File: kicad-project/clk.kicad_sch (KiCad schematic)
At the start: 7 parts, among them Q1 Q_NPN_BCE, U5 LM555xN

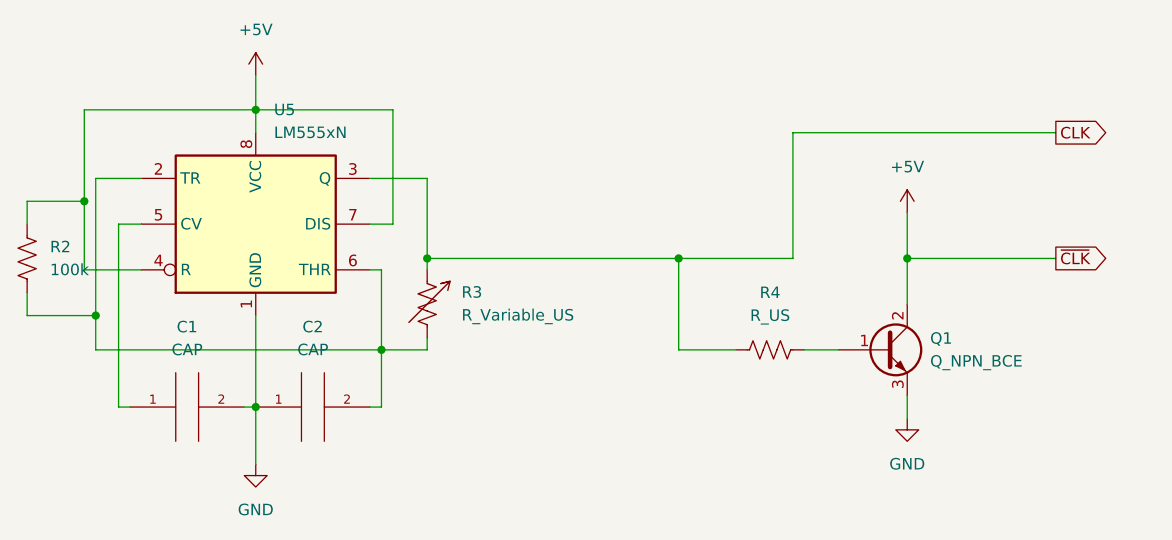
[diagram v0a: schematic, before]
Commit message: update schematic
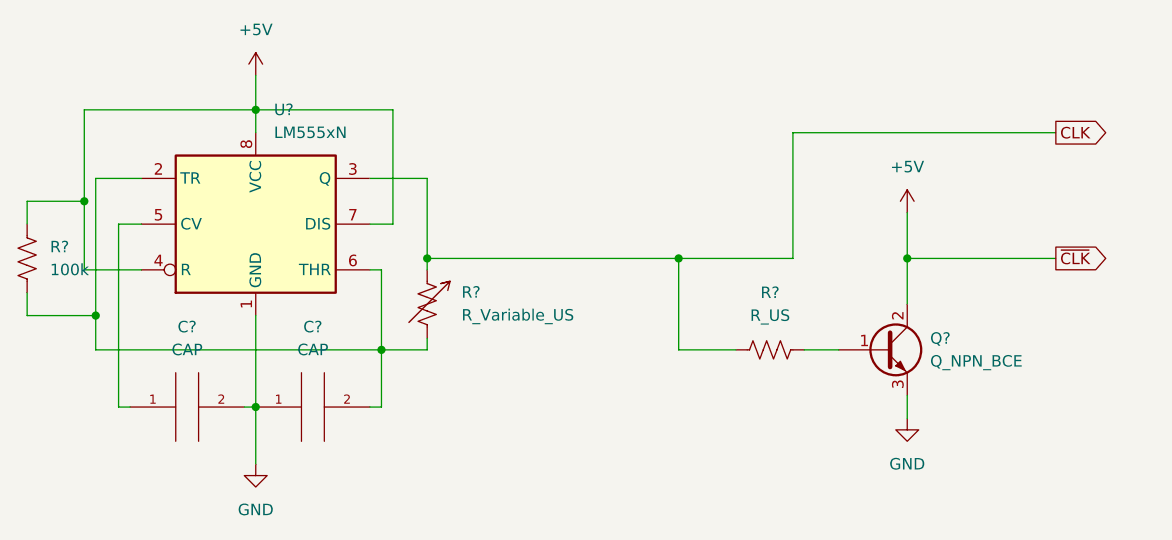
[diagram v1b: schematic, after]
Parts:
- renumbered C1 to C?, C2 to C?, Q1 to Q?, R3 to R?, R4 to R?, R2 to R?, U5 to U?
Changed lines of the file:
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@@
   (symbol (lib_id "power:GND") (at 152.4 128.27 0) (unit 1)
     (in_bom yes) (on_board yes) (fields_autoplaced)
-    (property "Reference" "#PWR0114" (id 0) (at 152.4 134.62 0)
+    (property "Reference" "#PWR0128" (id 0) (at 152.4 134.62 0)
       (effects (font (size 1.27 1.27)) hide)
     )
@@
   (symbol (lib_id "Timer:LM555xN") (at 152.4 101.6 0) (unit 1)
     (in_bom yes) (on_board yes) (fields_autoplaced)
-    (property "Reference" "U5" (id 0) (at 154.4194 88.9 0)
+    (property "Reference" "U?" (id 0) (at 154.4194 88.9 0)
       (effects (font (size 1.27 1.27)) (justify left))
     )
@@
   (symbol (lib_id "Device:R_Variable_US") (at 171.45 110.49 0) (unit 1)
     (in_bom yes) (on_board yes) (fields_autoplaced)
-    (property "Reference" "R3" (id 0) (at 175.26 109.1818 0)
+    (property "Reference" "R?" (id 0) (at 175.26 109.1818 0)
       (effects (font (size 1.27 1.27)) (justify left))
     )
@@
   (symbol (lib_id "Device:R_US") (at 209.55 115.57 90) (unit 1)
     (in_bom yes) (on_board yes) (fields_autoplaced)
-    (property "Reference" "R4" (id 0) (at 209.55 109.22 90))
+    (property "Reference" "R?" (id 0) (at 209.55 109.22 90))
     (property "Value" "R_US" (id 1) (at 209.55 111.76 90))
     (property "Footprint" "" (id 2) (at 209.804 114.554 90)
@@
   (symbol (lib_id "pspice:CAP") (at 144.78 121.92 90) (unit 1)
     (in_bom yes) (on_board yes) (fields_autoplaced)
-    (property "Reference" "C1" (id 0) (at 144.78 113.03 90))
+    (property "Reference" "C?" (id 0) (at 144.78 113.03 90))
     (property "Value" "CAP" (id 1) (at 144.78 115.57 90))
     (property "Footprint" "" (id 2) (at 144.78 121.92 0)
@@
   (symbol (lib_id "Device:Q_NPN_BCE") (at 222.25 115.57 0) (unit 1)
     (in_bom yes) (on_board yes) (fields_autoplaced)
-    (property "Reference" "Q1" (id 0) (at 227.33 114.2999 0)
+    (property "Reference" "Q?" (id 0) (at 227.33 114.2999 0)
       (effects (font (size 1.27 1.27)) (justify left))
     )
@@
   (symbol (lib_id "power:+5V") (at 224.79 100.33 0) (unit 1)
     (in_bom yes) (on_board yes) (fields_autoplaced)
-    (property "Reference" "#PWR0111" (id 0) (at 224.79 104.14 0)
+    (property "Reference" "#PWR0126" (id 0) (at 224.79 104.14 0)
       (effects (font (size 1.27 1.27)) hide)
     )
@@
   (symbol (lib_id "power:GND") (at 224.79 123.19 0) (unit 1)
     (in_bom yes) (on_board yes) (fields_autoplaced)
-    (property "Reference" "#PWR0112" (id 0) (at 224.79 129.54 0)
+    (property "Reference" "#PWR0125" (id 0) (at 224.79 129.54 0)
       (effects (font (size 1.27 1.27)) hide)
     )
@@
   (symbol (lib_id "Device:R_US") (at 127 105.41 0) (unit 1)
     (in_bom yes) (on_board yes) (fields_autoplaced)
-    (property "Reference" "R2" (id 0) (at 129.54 104.1399 0)
+    (property "Reference" "R?" (id 0) (at 129.54 104.1399 0)
       (effects (font (size 1.27 1.27)) (justify left))
     )
@@
   (symbol (lib_id "power:+5V") (at 152.4 85.09 0) (unit 1)
     (in_bom yes) (on_board yes) (fields_autoplaced)
-    (property "Reference" "#PWR0113" (id 0) (at 152.4 88.9 0)
+    (property "Reference" "#PWR0127" (id 0) (at 152.4 88.9 0)
       (effects (font (size 1.27 1.27)) hide)
     )
@@
   (symbol (lib_id "pspice:CAP") (at 158.75 121.92 90) (unit 1)
     (in_bom yes) (on_board yes) (fields_autoplaced)
-    (property "Reference" "C2" (id 0) (at 158.75 113.03 90))
+    (property "Reference" "C?" (id 0) (at 158.75 113.03 90))
     (property "Value" "CAP" (id 1) (at 158.75 115.57 90))
     (property "Footprint" "" (id 2) (at 158.75 121.92 0)
